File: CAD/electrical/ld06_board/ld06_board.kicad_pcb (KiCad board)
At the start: 2 copper layers, 9 parts, among them J1 RS485, J2 LED Strip, J3 Conn_01x04_Pin, J4 I2C, U1 MAX485E, U2 SeeeduinoXIAO

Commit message: update PCB
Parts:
- added J5: Conn_01x02_Pin, Connector_Molex:Molex_KK-254_AE-6410-02A_1x02_P2.54mm_Vertical, F.Cu at (64.4, 39.7)
- added J6: Conn_01x02_Pin, Connector_Molex:Molex_KK-254_AE-6410-02A_1x02_P2.54mm_Vertical, F.Cu at (71.6, 39.7)
- added J7: I2C, Connector_Molex:Molex_KK-254_AE-6410-04A_1x04_P2.54mm_Vertical, F.Cu at (27.4, 34.0)
- added J9: Battery in, Connector_BarrelJack:BarrelJack_Horizontal, F.Cu at (12.0, 19.8)
- added R2: R, Resistor_THT:R_Axial_DIN0309_L9.0mm_D3.2mm_P12.70mm_Horizontal, F.Cu at (50.6, 29.4)
- added U3: LM7805_TO220, Package_TO_SOT_THT:TO-220-3_Vertical, F.Cu at (70.5, 47.5)
- C2: footprint Capacitor_SMD:C_0603_1608Metric -> Resistor_THT:R_Axial_DIN0204_L3.6mm_D1.6mm_P5.08mm_Vertical
- J1: value RS485 -> SERIAL
- J3: value Conn_01x04_Pin -> Conn_01x02_Pin; footprint Connector_Molex:Molex_KK-254_AE-6410-04A_1x04_P2.54mm_Vertical -> Connector_Molex:Molex_KK-254_AE-6410-02A_1x02_P2.54mm_Vertical
- R1: value 120R -> R; footprint Resistor_SMD:R_0603_1608Metric -> Resistor_THT:R_Axial_DIN0309_L9.0mm_D3.2mm_P12.70mm_Horizontal
- U1: value MAX485E -> TXBN0304RUT; footprint Package_SO:SOIC-8_3.9x4.9mm_P1.27mm -> Package_DIP:DIP-12_W10.16mm
- moved J1 37.8 mm to (57.3, 47.5)
- moved C1 31.9 mm to (19.2, 14.0)
- moved C2 31.2 mm to (19.5, 20.0)
- moved J3 26.3 mm to (57.3, 39.7)
- moved R1 21.2 mm to (50.6, 18.9)
- moved J4 20.6 mm to (15.7, 30.3)
- moved U2 16.4 mm to (38.5, 18.5)
- moved U1 11.6 mm to (38.9, 38.1)
- moved J2 2.21 mm to (17.9, 39.9)
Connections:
- J1 pad 1: +5V -> /RX(ESP)
- J1 pad 2: Net-(J1-Pin_2) -> /TX(ESP)
- J1 pad 3: Net-(J1-Pin_3) -> GND
- J1 pad 4: GND -> +5V
- J3 pad 1: unconnected-(J3-Pin_1-Pad1) -> /BTN1
- J3 pad 2: unconnected-(J3-Pin_2-Pad2) -> GND
- R1 pad 1: Net-(J1-Pin_3) -> unconnected-(R1-Pad1)
- R1 pad 2: Net-(J1-Pin_2) -> unconnected-(R1-Pad2)
- U1 pad 1: /UART_RXD -> unconnected-(U1-VCCA-Pad1)
- U1 pad 2: /RS485_TXE -> unconnected-(U1-A1-Pad2)
- U1 pad 3: /RS485_TXE -> unconnected-(U1-A2-Pad3)
- U1 pad 4: /UART_TXD -> unconnected-(U1-A3-Pad4)
- U1 pad 5: GND -> unconnected-(U1-A4-Pad5)
- U1 pad 6: Net-(J1-Pin_2) -> unconnected-(U1-GND-Pad6)
- U1 pad 7: Net-(J1-Pin_3) -> unconnected-(U1-B4-Pad7)
- U1 pad 8: +5V -> unconnected-(U1-B3-Pad8)
- U2 pad 7: unconnected-(U2-PB08_A6_D6_TX-Pad7)_1 -> /BTN1
- U2 pad 9: unconnected-(U2-PA7_A8_D8_SCK-Pad9)_1 -> /BTN2

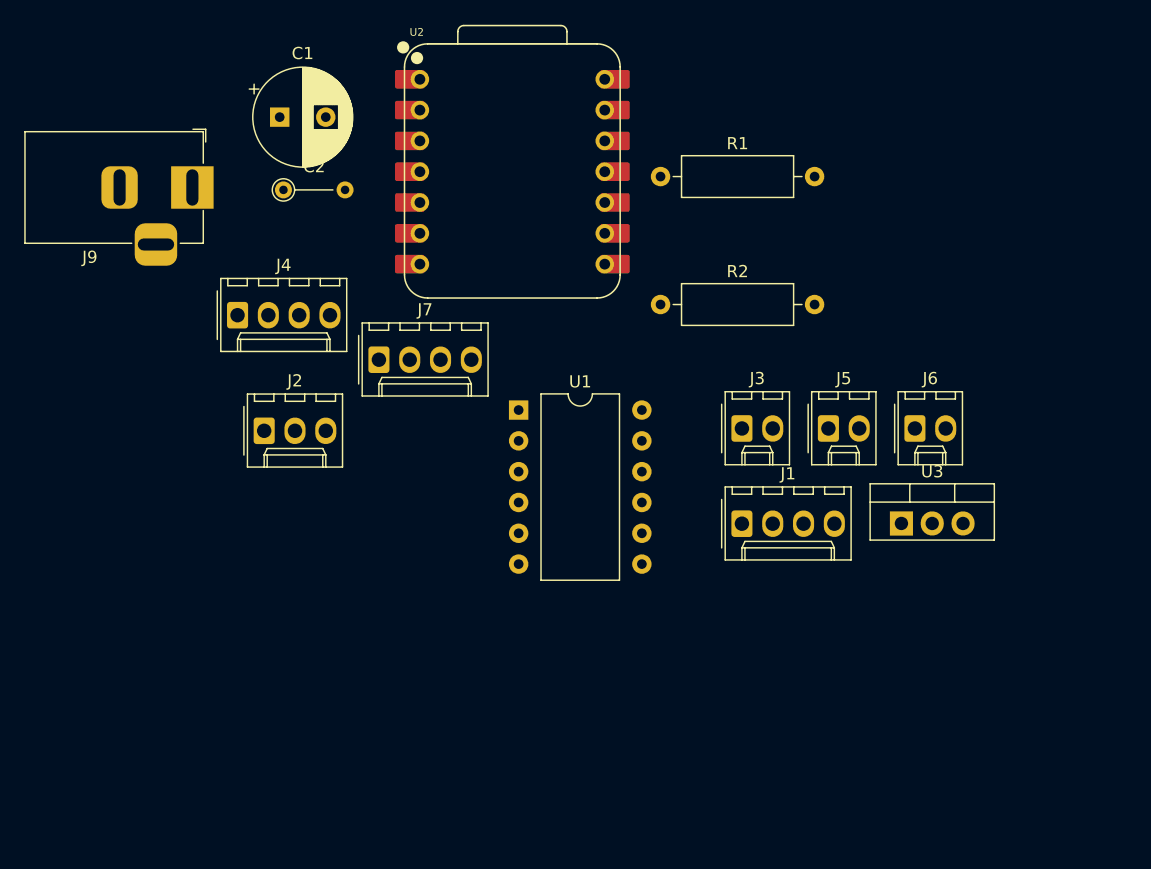
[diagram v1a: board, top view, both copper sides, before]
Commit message: LD06 board colplet
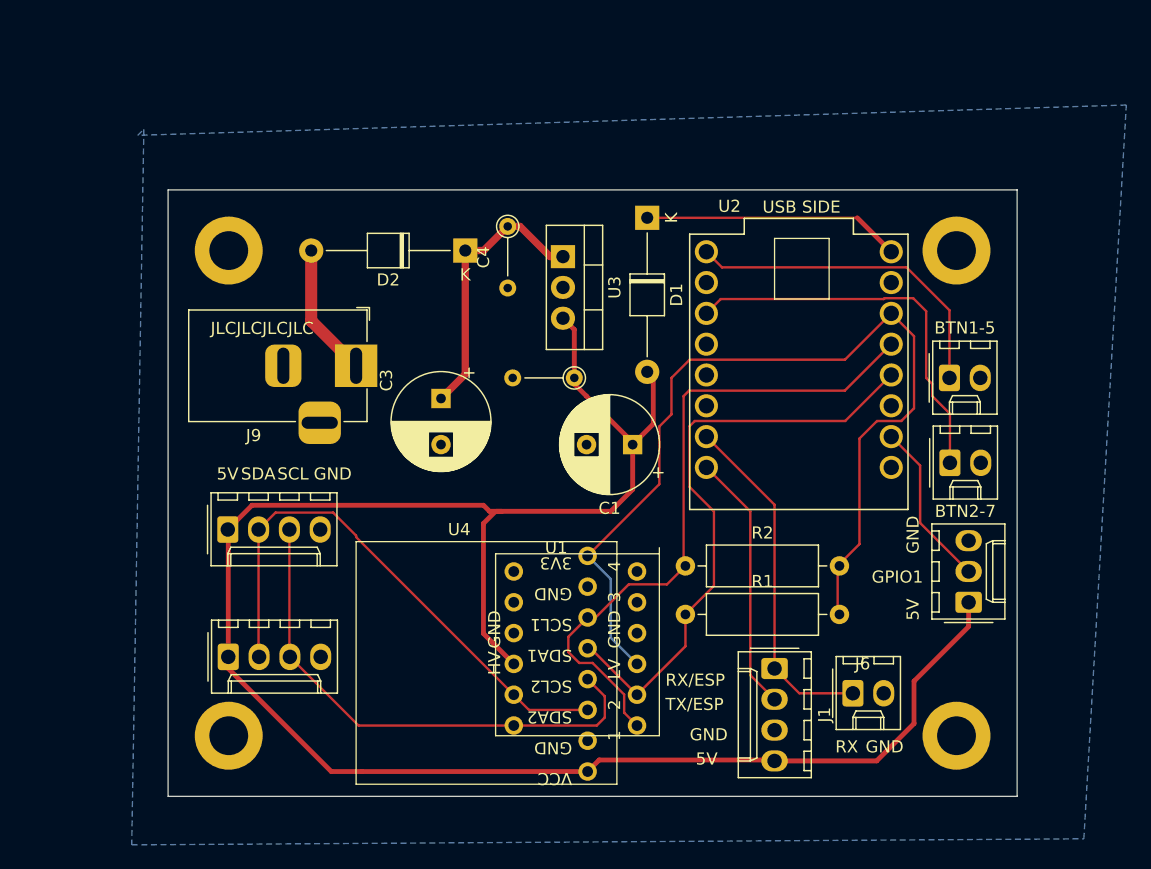
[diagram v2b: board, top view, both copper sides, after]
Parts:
- added C3: 10u, Capacitor_THT:CP_Radial_D8.0mm_P3.80mm, F.Cu at (32.5, 37.2)
- added C4: 100n, Resistor_THT:R_Axial_DIN0204_L3.6mm_D1.6mm_P5.08mm_Vertical, F.Cu at (38.0, 23.0)
- added D1: 1N4007, Diode_THT:D_T-1_P12.70mm_Horizontal, F.Cu at (49.5, 22.3)
- added D2: 1N4007, Diode_THT:D_T-1_P12.70mm_Horizontal, F.Cu at (34.5, 25.0)
- added REF**: MountingHole_3.2mm_M3_DIN965_Pad, MountingHole:MountingHole_3.2mm_M3_DIN965_Pad, F.Cu at (75.0, 65.0)
- added REF**: MountingHole_3.2mm_M3_DIN965_Pad, MountingHole:MountingHole_3.2mm_M3_DIN965_Pad, F.Cu at (15.0, 25.0)
- added REF**: MountingHole_3.2mm_M3_DIN965_Pad, MountingHole:MountingHole_3.2mm_M3_DIN965_Pad, F.Cu at (75.0, 25.0)
- added REF**: MountingHole_3.2mm_M3_DIN965_Pad, MountingHole:MountingHole_3.2mm_M3_DIN965_Pad, F.Cu at (15.0, 65.0)
- added U4: TXBN0304RUT, Level_shifter_library:PCA9306_ali, F.Cu at (44.6, 68.0)
- U1: footprint Package_DIP:DIP-12_W10.16mm -> Level_shifter_library:I2C_ali_level_shifter
- U2: value SeeeduinoXIAO -> ESP32-C3_SUPERMINI_TH; footprint Seeeduino XIAO KICAD:XIAO-ESP32-C3-DIP -> ESP32C3MINI:MODULE_ESP32-C3_SUPERMINI
- moved J2 59.8 mm to (76.0, 54.0), turned to 90 degrees
- moved C1 39.7 mm to (48.3, 41.0), turned to 180 degrees
- moved R1 36.2 mm to (52.6, 55.0)
- moved U3 35.5 mm to (42.6, 25.5), turned to -90 degrees
- moved U2 28.7 mm to (62.0, 35.0)
- moved C2 28.6 mm to (43.5, 35.5), turned to 180 degrees
- moved J4 28.2 mm to (15.0, 58.5)
- moved J6 22.4 mm to (66.5, 61.5)
- moved R2 21.6 mm to (52.6, 51.0)
- moved J9 20.0 mm to (25.5, 34.5)
- moved J7 18.7 mm to (14.9, 48.0)
- moved BTN1-5 17.6 mm to (74.4, 35.5)
- moved J1 12.2 mm to (60.0, 59.5), turned to -90 degrees
- moved U1 11.2 mm to (36.0, 48.9), turned to -90 degrees
- moved BTN2-7 10.4 mm to (74.5, 42.5)
- renumbered J3 to BTN1-5, J5 to BTN2-7
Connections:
- J9 pad 1: +12V -> Net-(D2-A)
- R1 pad 1: unconnected-(R1-Pad1) -> /3V3_SDA
- R1 pad 2: unconnected-(R1-Pad2) -> +3V3
- R2 pad 1: unconnected-(R2-Pad1) -> /3V3_SCL
- R2 pad 2: unconnected-(R2-Pad2) -> +3V3
- U1 pad 1: unconnected-(U1-VCCA-Pad1) -> +5V
- U1 pad 10: unconnected-(U1-B1-Pad10) -> /3V3_SCL
- U1 pad 11: unconnected-(U1-VCCB-Pad11) -> +3V3
- U1 pad 2: unconnected-(U1-A1-Pad2) -> /I2C_SCL
- U1 pad 3: unconnected-(U1-A2-Pad3) -> /I2C_SDA
- U1 pad 6: unconnected-(U1-GND-Pad6) -> GND
- U1 pad 9: unconnected-(U1-B2-Pad9) -> /3V3_SDA
- U2 pad 1: /UART_RXD -> /LED_DIG
- U2 pad 10: /LIDAR_PWM -> unconnected-(U2-GPIO10-Pad10)
- U2 pad 2: /RS485_TXE -> unconnected-(U2-GPIO2-Pad2)
- U2 pad 3: /UART_TXD -> /3V3_SDA
- U2 pad 4: /LED_DIG -> /3V3_SCL
- U2 pad 5: /I2C_SDA -> /BTN1
- U2 pad 6: /I2C_SCL -> unconnected-(U2-GPIO6-Pad6)
- U2 pad 7: /BTN1 -> /BTN2
- U2 pad 8: /LIDAR_TX -> unconnected-(U2-GPIO8-Pad8)
- U2 pad 9: /BTN2 -> unconnected-(U2-GPIO9-Pad9)
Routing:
- net +5V: track 0.00 -> 158.2 mm
- net +3V3: track 0.00 -> 78.5 mm
- net /3V3_SCL: track 0.00 -> 55.2 mm
- net /3V3_SDA: track 0.00 -> 49.6 mm
- net /I2C_SDA: track 0.00 -> 45.7 mm
- net /I2C_SCL: track 0.00 -> 43.3 mm
- net /BTN2: track 0.00 -> 32.4 mm
- net /RX(ESP): track 0.00 -> 28.8 mm
- net /BTN1: track 0.00 -> 27.6 mm
- net +12V: track 0.00 -> 22.9 mm
- net /TX(ESP): track 0.00 -> 21.4 mm
- net Net-(D1-K): track 0.00 -> 21.3 mm
- net /LED_DIG: track 0.00 -> 13.8 mm
- net Net-(D2-A): track 0.00 -> 11.0 mm
- added copper zone on B.Cu, net GND
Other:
- board outline added: 70 x 50 mm
- board text added: "5V"
- board text added: "GND"
- board text added: "GPIO1"
- board text added: "JLCJLCJLCJLC"
- board text added: "RX"
- board text added: "RX/ESP"
- board text added: "SCL"
- board text added: "SDA"
- board text added: "TX/ESP"
- board text added: "USB SIDE"
